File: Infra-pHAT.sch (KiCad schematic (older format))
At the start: 20 parts, among them Q1 BC817, U1 CAT24C32WI-GT3

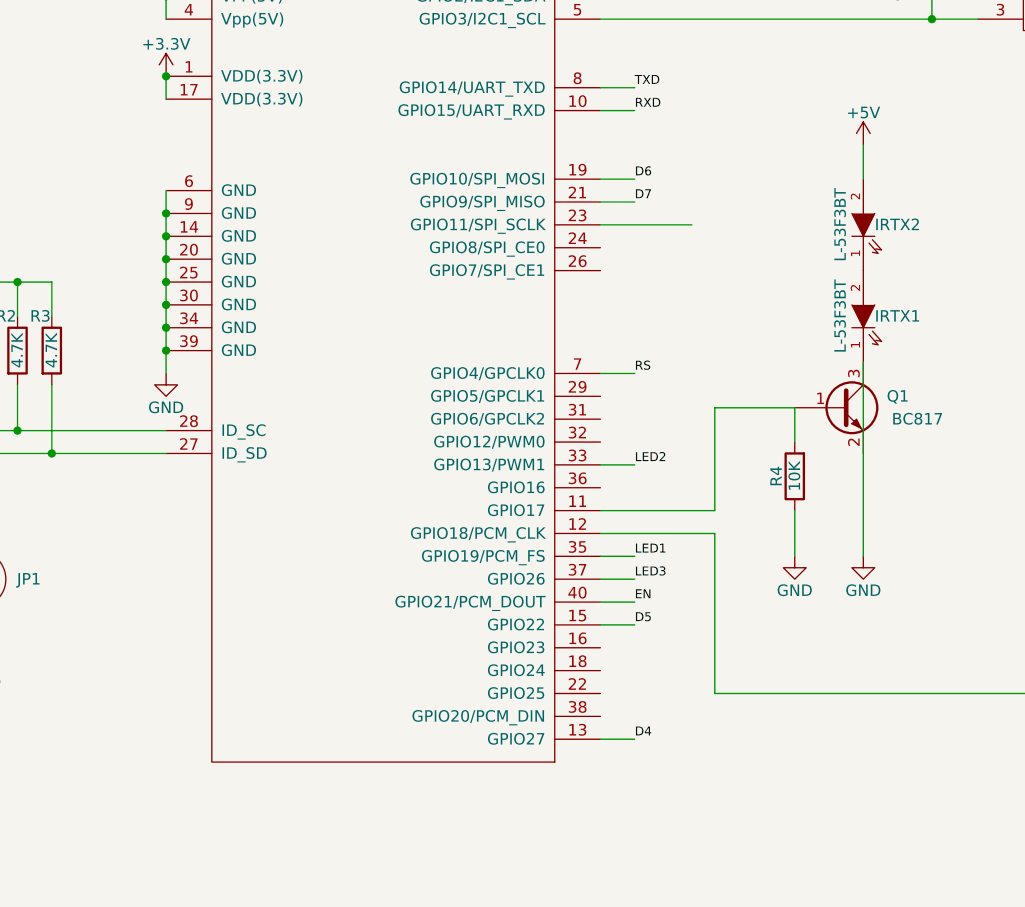
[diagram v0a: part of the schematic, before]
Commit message: Fix position of mounting holes and pin header
Fix wiring of transistor for IR leds

Signed-off-by: Rangel Ivanov <rangelivanov88@gmail.com>
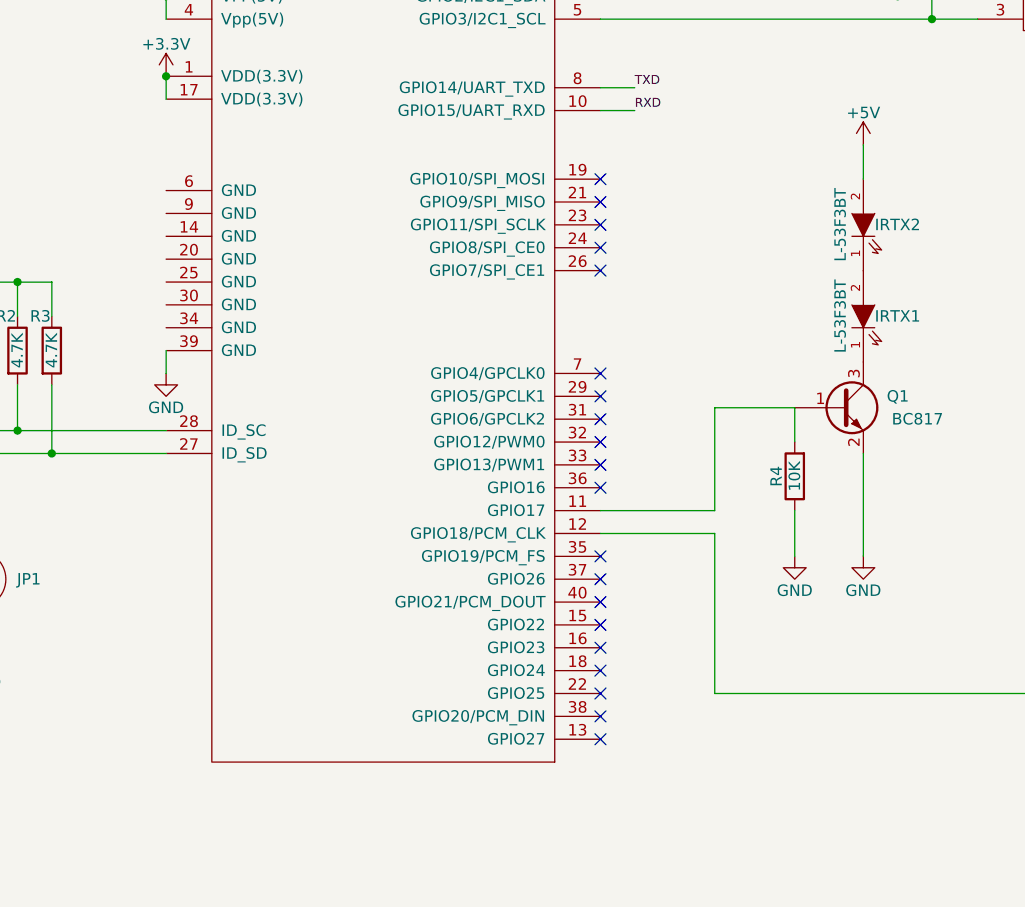
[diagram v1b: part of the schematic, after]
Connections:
- net GND: now also Q1.2 (E); no longer IRTX1.1 (K), Q1.3 (C), RASP_CONN1.14 (GND), RASP_CONN1.20 (GND), RASP_CONN1.25 (GND), RASP_CONN1.30 (GND), RASP_CONN1.34 (GND), RASP_CONN1.6 (GND), RASP_CONN1.9 (GND)
- net D4: no longer names the net of RASP_CONN1.13 (GPIO27)
- net D5: no longer names the net of RASP_CONN1.15 (GPIO22)
- net D6: no longer names the net of RASP_CONN1.19 (GPIO10/SPI_MOSI)
- net D7: no longer names the net of RASP_CONN1.21 (GPIO9/SPI_MISO)
- net EN: no longer names the net of RASP_CONN1.40 (GPIO21/PCM_DOUT)
- net LED1: no longer names the net of RASP_CONN1.35 (GPIO19/PCM_FS)
- net LED2: no longer names the net of RASP_CONN1.33 (GPIO13/PWM1)
- net LED3: no longer names the net of RASP_CONN1.37 (GPIO26)
- net RS: no longer names the net of RASP_CONN1.7 (GPIO4/GPCLK0)
- new net: IRTX1.1 (K), Q1.3 (C)
- no-connect marks 0 -> 20
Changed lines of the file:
@@
 EESchema Schematic File Version 2
-LIBS:power
-LIBS:device
-LIBS:transistors
-LIBS:conn
-LIBS:linear
-LIBS:regul
-LIBS:74xx
-LIBS:cmos4000
-LIBS:adc-dac
-LIBS:memory
-LIBS:xilinx
-LIBS:microcontrollers
-LIBS:dsp
-LIBS:microchip
-LIBS:analog_switches
-LIBS:motorola
-LIBS:texas
-LIBS:intel
-LIBS:audio
-LIBS:interface
-LIBS:digital-audio
-LIBS:philips
-LIBS:display
-LIBS:cypress
-LIBS:siliconi
-LIBS:opto
-LIBS:atmel
-LIBS:contrib
-LIBS:valves
 LIBS:mylibrary
 LIBS:Infra-pHAT-cache
@@
 $EndComp
 Wire Wire Line
-	3450 2650 3450 3450
-Connection ~ 3450 2750
-Connection ~ 3450 2850
-Connection ~ 3450 2950
-Connection ~ 3450 3050
-Connection ~ 3450 3150
-Connection ~ 3450 3250
-Connection ~ 3450 3350
-Wire Wire Line
 	3450 2150 3450 2250
 Connection ~ 3450 2150
@@
 	0    1    1    0
 $EndComp
-Wire Wire Line
-	6500 3400 6500 4250
 $Comp
 L R R4
@@
 	7850 5150 7900 5150
 Wire Wire Line
-	5350 4550 5500 4550
-Wire Wire Line
-	5350 3850 5500 3850
-Text Label 5500 4550 0    39   ~ 0
-D5
-Wire Wire Line
 	7550 5150 7500 5150
 Wire Wire Line
@@
 	7400 4850 7400 4750
 Wire Wire Line
-	5350 2800 5750 2800
-Wire Wire Line
-	5350 5050 5500 5050
-Text Label 5500 5050 0    39   ~ 0
-D4
-Wire Wire Line
-	5350 2600 5500 2600
-Text Label 5500 2600 0    39   ~ 0
-D6
-Wire Wire Line
-	5350 2700 5500 2700
-Text Label 5500 2700 0    39   ~ 0
-D7
-Wire Wire Line
 	6500 2450 6500 2600
-Wire Wire Line
-	5350 4250 5500 4250
-Text Label 5500 4250 0    39   ~ 0
-LED1
-Text Label 5500 3850 0    39   ~ 0
-LED2
-Wire Wire Line
-	5350 4350 5500 4350
-Text Label 5500 4350 0    39   ~ 0
-LED3
-Wire Wire Line
-	5350 4450 5500 4450
-Text Label 5500 4450 0    39   ~ 0
-EN
 $Comp
 L CONN_01X04 UART1
@@
 	5850 4050 5350 4050
 Wire Wire Line
-	5350 3450 5500 3450
-Text Label 5500 3450 0    39   ~ 0
-RS
-Wire Wire Line
 	6800 900  6800 1900
 Wire Wire Line
@@
 Wire Wire Line
 	6200 4050 6200 4250
+Wire Wire Line
+	6500 3800 6500 4250
+NoConn ~ 5350 5050
+NoConn ~ 5350 4950
+NoConn ~ 5350 4850
+NoConn ~ 5350 4750
+NoConn ~ 5350 4650
+NoConn ~ 5350 4550
+NoConn ~ 5350 4450
+NoConn ~ 5350 4350
+NoConn ~ 5350 4250
+NoConn ~ 5350 3550
+NoConn ~ 5350 3650
+NoConn ~ 5350 3750
+NoConn ~ 5350 3850
+NoConn ~ 5350 3950
+NoConn ~ 5350 3450
+NoConn ~ 5350 2900
+NoConn ~ 5350 3000
+NoConn ~ 5350 2800
+NoConn ~ 5350 2600
+NoConn ~ 5350 2700
+Wire Wire Line
+	3450 3350 3450 3450
 $EndSCHEMATC

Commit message: Add filled zone for front layer (GND net)
Route RX/TX for UART connector

Signed-off-by: Rangel Ivanov <rangelivanov88@gmail.com>
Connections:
- net GND: now also RASP_CONN1.14 (GND), RASP_CONN1.20 (GND), RASP_CONN1.25 (GND), RASP_CONN1.30 (GND), RASP_CONN1.34 (GND), RASP_CONN1.6 (GND), RASP_CONN1.9 (GND)
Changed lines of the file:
@@
 	1    0    0    -1
 $EndComp
-Wire Wire Line
-	950  3500 800  3500
-Wire Wire Line
-	800  3500 800  3950
-Wire Wire Line
-	950  3600 800  3600
-Connection ~ 800  3600
-Wire Wire Line
-	950  3700 800  3700
-Connection ~ 800  3700
-Wire Wire Line
-	950  3800 800  3800
-Connection ~ 800  3800
 $Comp
 L GND #PWR02
@@
 	0    1    1    0
 $EndComp
-Wire Wire Line
-	2200 3500 2050 3500
 $Comp
 L +3.3V #PWR03
@@
 	1    0    0    -1
 $EndComp
-Connection ~ 2200 3050
-Wire Wire Line
-	2950 3050 2950 3200
-Wire Wire Line
-	2800 3050 2800 3200
-Connection ~ 2800 3050
-Wire Wire Line
-	2650 3200 2650 3050
-Connection ~ 2650 3050
-Wire Wire Line
-	2200 3050 2950 3050
-Wire Wire Line
-	2050 3600 2650 3600
-Wire Wire Line
-	2650 3500 2650 4050
-Wire Wire Line
-	2800 3700 2800 3500
-Wire Wire Line
-	2950 3800 2950 3500
 $Comp
 L GND #PWR04
@@
 	1    0    0    -1
 $EndComp
-Connection ~ 2950 3800
-Connection ~ 2800 3700
 $Comp
 L Raspberry_PI RASP_CONN1
@@
 	1    0    0    -1
 $EndComp
-Wire Wire Line
-	2200 2700 2200 3500
-Connection ~ 2650 3600
 $Comp
 L LED IRTX1
@@
 	0    1    1    0
 $EndComp
-Wire Wire Line
-	7500 4750 7500 5300
 $Comp
 L CP C2
@@
 	1    0    0    -1
 $EndComp
-Connection ~ 7500 5150
 $Comp
 L +3.3V #PWR08
@@
 	1    0    0    -1
 $EndComp
-Wire Wire Line
-	3450 2150 3450 2250
-Connection ~ 3450 2150
 $Comp
 L +3.3V #PWR010
@@
 	1    0    0    -1
 $EndComp
-Connection ~ 3450 1800
 $Comp
 L +5V #PWR011
@@
 	1    0    0    -1
 $EndComp
-Wire Wire Line
-	3450 1800 3450 1900
 $Comp
 L I2C_SENS_1 SENS1
@@
 	1    0    0    -1
 $EndComp
-Wire Wire Line
-	5350 1800 7000 1800
-Wire Wire Line
-	5350 1900 7000 1900
-Connection ~ 6650 1800
-Connection ~ 6800 1900
 $Comp
 L GND #PWR012
@@
 	1    0    0    -1
 $EndComp
-Wire Wire Line
-	8050 900  8050 2100
-Wire Wire Line
-	8050 1900 7900 1900
 $Comp
 L +3.3V #PWR013
@@
 	1    0    0    -1
 $EndComp
-Connection ~ 7900 1800
 $Comp
 L Q_NPN_BEC Q1
@@
 	-1   0    0    1
 $EndComp
-Wire Wire Line
-	2050 3700 3450 3700
-Wire Wire Line
-	2050 3800 3450 3800
-Wire Wire Line
-	7850 5150 7900 5150
-Wire Wire Line
-	7550 5150 7500 5150
-Wire Wire Line
-	5350 4150 5850 4150
-Wire Wire Line
-	5850 4150 5850 4850
-Wire Wire Line
-	5850 4850 7400 4850
-Wire Wire Line
-	7400 4850 7400 4750
-Wire Wire Line
-	6500 2450 6500 2600
 $Comp
 L CONN_01X04 UART1
@@
 	1    0    0    -1
 $EndComp
-Wire Wire Line
-	8800 2400 8550 2400
 $Comp
 L GND #PWR015
@@
 	1    0    0    -1
 $EndComp
-Wire Wire Line
-	8550 2100 8800 2100
-Wire Wire Line
-	5350 2200 5500 2200
 Text Label 5500 2200 0    39   ~ 0
 TXD
-Wire Wire Line
-	5350 2300 5500 2300
 Text Label 5500 2300 0    39   ~ 0
 RXD
-Wire Wire Line
-	8800 2200 8550 2200
 Text Label 8550 2200 0    39   ~ 0
 TXD
-Wire Wire Line
-	8800 2300 8550 2300
 Text Label 8550 2300 0    39   ~ 0
 RXD
@@
 	1    0    0    -1
 $EndComp
-Connection ~ 7900 1200
-Connection ~ 7900 800
-Wire Wire Line
-	7900 900  8050 900
-Wire Wire Line
-	8050 1300 7900 1300
-Connection ~ 8050 1900
-Connection ~ 8050 1300
-Wire Wire Line
-	7000 800  6650 800
-Wire Wire Line
-	6200 1200 7000 1200
-Connection ~ 6650 1200
-Wire Wire Line
-	7000 900  6800 900
-Wire Wire Line
-	6350 1300 7000 1300
-Connection ~ 6800 1300
-Wire Wire Line
-	6350 1050 6350 1300
-Wire Wire Line
-	6200 1050 6200 1200
-Wire Wire Line
-	6050 750  6350 750
-Connection ~ 6200 750
 $Comp
 L +3.3V #PWR017
@@
 	0    -1   -1   0
 $EndComp
-Wire Wire Line
-	5850 4050 5350 4050
-Wire Wire Line
-	6800 900  6800 1900
-Wire Wire Line
-	6650 800  6650 1800
-Wire Wire Line
-	7900 700  7900 1800
 $Comp
 L LED IRTX2
@@
 	0    -1   -1   0
 $EndComp
-Wire Wire Line
-	5850 4050 5850 3600
-Wire Wire Line
-	5850 3600 6200 3600
-Wire Wire Line
-	6200 3600 6200 3750
 $Comp
 L GND #PWR018
@@
 	1    0    0    -1
 $EndComp
-Wire Wire Line
-	6200 4050 6200 4250
-Wire Wire Line
-	6500 3800 6500 4250
 NoConn ~ 5350 5050
 NoConn ~ 5350 4950
@@
 NoConn ~ 5350 2700
 Wire Wire Line
-	3450 3350 3450 3450
+	950  3500 800  3500
+Wire Wire Line
+	800  3500 800  3950
+Wire Wire Line
+	950  3600 800  3600
+Connection ~ 800  3600
+Wire Wire Line
+	950  3700 800  3700
+Connection ~ 800  3700
+Wire Wire Line
+	950  3800 800  3800
+Connection ~ 800  3800
+Wire Wire Line
+	2200 3500 2050 3500
+Connection ~ 2200 3050
+Wire Wire Line
+	2950 3050 2950 3200
+Wire Wire Line
+	2800 3050 2800 3200
+Connection ~ 2800 3050
+Wire Wire Line
+	2650 3200 2650 3050
+Connection ~ 2650 3050
+Wire Wire Line
+	2200 3050 2950 3050
+Wire Wire Line
+	2050 3600 2650 3600
+Wire Wire Line
+	2650 3500 2650 4050
+Wire Wire Line
+	2800 3700 2800 3500
+Wire Wire Line
+	2950 3800 2950 3500
+Connection ~ 2950 3800
+Connection ~ 2800 3700
+Wire Wire Line
+	2200 2700 2200 3500
+Connection ~ 2650 3600
+Wire Wire Line
+	7500 4750 7500 5300
+Connection ~ 7500 5150
+Wire Wire Line
+	3450 2150 3450 2250
+Connection ~ 3450 2150
+Connection ~ 3450 1800
+Wire Wire Line
+	3450 1800 3450 1900
+Wire Wire Line
+	5350 1800 7000 1800
+Wire Wire Line
+	5350 1900 7000 1900
+Connection ~ 6650 1800
+Connection ~ 6800 1900
+Wire Wire Line
+	8050 900  8050 2100
+Wire Wire Line
+	8050 1900 7900 1900
+Connection ~ 7900 1800
+Wire Wire Line
+	2050 3700 3450 3700
+Wire Wire Line
+	2050 3800 3450 3800
+Wire Wire Line
+	7850 5150 7900 5150
+Wire Wire Line
+	7550 5150 7500 5150
+Wire Wire Line
+	5350 4150 5850 4150
+Wire Wire Line
+	5850 4150 5850 4850
+Wire Wire Line
+	5850 4850 7400 4850
+Wire Wire Line
+	7400 4850 7400 4750
+Wire Wire Line
+	6500 2450 6500 2600
+Wire Wire Line
+	8800 2400 8550 2400
+Wire Wire Line
+	8550 2100 8800 2100
+Wire Wire Line
+	5350 2200 5500 2200
+Wire Wire Line
+	5350 2300 5500 2300
+Wire Wire Line
+	8800 2200 8550 2200
+Wire Wire Line
+	8800 2300 8550 2300
+Connection ~ 7900 1200
+Connection ~ 7900 800
+Wire Wire Line
+	7900 900  8050 900
+Wire Wire Line
+	8050 1300 7900 1300
+Connection ~ 8050 1900
+Connection ~ 8050 1300
+Wire Wire Line
+	7000 800  6650 800
+Wire Wire Line
+	6200 1200 7000 1200
+Connection ~ 6650 1200
+Wire Wire Line
+	7000 900  6800 900
+Wire Wire Line
+	6350 1300 7000 1300
+Connection ~ 6800 1300
+Wire Wire Line
+	6350 1050 6350 1300
+Wire Wire Line
+	6200 1050 6200 1200
+Wire Wire Line
+	6050 750  6350 750
+Connection ~ 6200 750
+Wire Wire Line
+	5850 4050 5350 4050
+Wire Wire Line
+	6800 900  6800 1900
+Wire Wire Line
+	6650 800  6650 1800
+Wire Wire Line
+	7900 700  7900 1800
+Wire Wire Line
+	5850 4050 5850 3600
+Wire Wire Line
+	5850 3600 6200 3600
+Wire Wire Line
+	6200 3600 6200 3750
+Wire Wire Line
+	6200 4050 6200 4250
+Wire Wire Line
+	6500 3800 6500 4250
+Wire Wire Line
+	3450 2650 3450 3450
+Connection ~ 3450 2750
+Connection ~ 3450 2850
+Connection ~ 3450 2950
+Connection ~ 3450 3050
+Connection ~ 3450 3150
+Connection ~ 3450 3350
+Connection ~ 3450 3250
 $EndSCHEMATC

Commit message: Infra-pHAT.pro: remap symbols
Remap KiCad symbols.

Signed-off-by: Leon Anavi <leon@anavi.org>
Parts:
- C1: symbol C -> Infra-pHAT-rescue:C
- C2: symbol CP -> Infra-pHAT-rescue:CP
- IRRX1: symbol TSOP382 -> mylibrary:TSOP382
- IRTX1, IRTX2: symbol LED -> Infra-pHAT-rescue:LED
- JP1: symbol JUMPER -> Infra-pHAT-rescue:JUMPER
- Q1: symbol Q_NPN_BEC -> Infra-pHAT-rescue:Q_NPN_BEC
- R1, R2, R3, R4, R5, R6, R7: symbol R -> Infra-pHAT-rescue:R
- RASP_CONN1: symbol Raspberry_PI -> mylibrary:Raspberry_PI
- SENS1, SENS2, SENS3: symbol I2C_SENS_1 -> mylibrary:I2C_SENS_1
- U1: symbol CAT24C32WI-GT3 -> mylibrary:CAT24C32WI-GT3
- UART1: symbol CONN_01X04 -> Infra-pHAT-rescue:CONN_01X04
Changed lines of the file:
@@
-EESchema Schematic File Version 2
-LIBS:mylibrary
-LIBS:Infra-pHAT-cache
-EELAYER 25 0
+EESchema Schematic File Version 4
+EELAYER 30 0
 EELAYER END
 $Descr A4 11693 8268
@@
 $EndDescr
 $Comp
-L CAT24C32WI-GT3 U1
+L mylibrary:CAT24C32WI-GT3 U1
 U 1 1 56FB5761
 P 1500 3300
@@
 $EndComp
 $Comp
-L R R1
+L Infra-pHAT-rescue:R R1
 U 1 1 56FB57DD
 P 2650 3350
@@
 $EndComp
 $Comp
-L R R2
+L Infra-pHAT-rescue:R R2
 U 1 1 56FB589D
 P 2800 3350
@@
 $EndComp
 $Comp
-L R R3
+L Infra-pHAT-rescue:R R3
 U 1 1 56FB5912
 P 2950 3350
@@
 $EndComp
 $Comp
-L C C1
+L Infra-pHAT-rescue:C C1
 U 1 1 56FB5967
 P 2050 3050
@@
 $EndComp
 $Comp
-L GND #PWR01
+L power:GND #PWR01
 U 1 1 56FB5AA8
 P 800 3950
@@
 $EndComp
 $Comp
-L GND #PWR02
+L power:GND #PWR02
 U 1 1 56FB5B93
 P 1900 3050
@@
 $EndComp
 $Comp
-L +3.3V #PWR03
+L power:+3.3V #PWR03
 U 1 1 56FB5F37
 P 2200 2700
@@
 $EndComp
 $Comp
-L GND #PWR04
+L power:GND #PWR04
 U 1 1 56FB60BD
 P 2650 4650
@@
 $EndComp
 $Comp
-L Raspberry_PI RASP_CONN1
+L mylibrary:Raspberry_PI RASP_CONN1
 U 1 1 56FB7C7A
 P 4400 1700
@@
 $EndComp
 $Comp
-L LED IRTX1
+L Infra-pHAT-rescue:LED IRTX1
 U 1 1 56FCCD5F
 P 6500 3200
@@
 $EndComp
 $Comp
-L GND #PWR05
+L power:GND #PWR05
 U 1 1 56FCD5E9
 P 6500 4250
@@
 $EndComp
 $Comp
-L TSOP382 IRRX1
+L mylibrary:TSOP382 IRRX1
 U 1 1 56FCDD28
 P 7250 4550
@@
 $EndComp
 $Comp
-L GND #PWR06
+L power:GND #PWR06
 U 1 1 56FCDFD8
 P 7600 4750
@@
 $EndComp
 $Comp
-L R R5
+L Infra-pHAT-rescue:R R5
 U 1 1 56FCE3CD
 P 7700 5150
@@
 $EndComp
 $Comp
-L CP C2
+L Infra-pHAT-rescue:CP C2
 U 1 1 56FCE773
 P 7500 5450
@@
 $EndComp
 $Comp
-L GND #PWR07
+L power:GND #PWR07
 U 1 1 56FCE7D8
 P 7500 5600
@@
 $EndComp
 $Comp
-L +3.3V #PWR08
+L power:+3.3V #PWR08
 U 1 1 56FCEA80
 P 7900 5150
@@
 $EndComp
 $Comp
-L GND #PWR09
+L power:GND #PWR09
 U 1 1 56FD1B71
 P 3450 3450
@@
 $EndComp
 $Comp
-L +3.3V #PWR010
+L power:+3.3V #PWR010
 U 1 1 56FD2267
 P 3450 2150
@@
 $EndComp
 $Comp
-L +5V #PWR011
+L power:+5V #PWR011
 U 1 1 56FF1D94
 P 3450 1800
@@
 $EndComp
 $Comp
-L I2C_SENS_1 SENS1
+L mylibrary:I2C_SENS_1 SENS1
 U 1 1 5704A9C3
 P 7200 1700
@@
 $EndComp
 $Comp
-L GND #PWR012
+L power:GND #PWR012
 U 1 1 5704B80C
 P 8050 2100
@@
 $EndComp
 $Comp
-L +3.3V #PWR013
+L power:+3.3V #PWR013
 U 1 1 5704BA43
 P 7900 700
@@
 $EndComp
 $Comp
-L Q_NPN_BEC Q1
+L Infra-pHAT-rescue:Q_NPN_BEC Q1
 U 1 1 570BF19F
 P 6400 3600
@@
 $EndComp
 $Comp
-L +5V #PWR014
+L power:+5V #PWR014
 U 1 1 570BFB30
 P 6500 2450
@@
 $EndComp
 $Comp
-L R R6
+L Infra-pHAT-rescue:R R6
 U 1 1 570C0762
 P 6200 900
@@
 $EndComp
 $Comp
-L R R7
+L Infra-pHAT-rescue:R R7
 U 1 1 570C0BD5
 P 6350 900
@@
 $EndComp
 $Comp
-L JUMPER JP1
+L Infra-pHAT-rescue:JUMPER JP1
 U 1 1 570C5478
 P 2650 4350
@@
 $EndComp
 $Comp
-L R R4
+L Infra-pHAT-rescue:R R4
 U 1 1 570BEF32
 P 6200 3900
@@
 $EndComp
 $Comp
-L CONN_01X04 UART1
+L Infra-pHAT-rescue:CONN_01X04 UART1
 U 1 1 574EB04E
 P 9000 2250
@@
 $EndComp
 $Comp
-L GND #PWR015
+L power:GND #PWR015
 U 1 1 574EBFC1
 P 8550 2400
@@
 $EndComp
 $Comp
-L +3.3V #PWR016
+L power:+3.3V #PWR016
 U 1 1 574EC177
 P 8550 2100
@@
 RXD
 $Comp
-L I2C_SENS_1 SENS2
+L mylibrary:I2C_SENS_1 SENS2
 U 1 1 5752A123
 P 7200 1100
@@
 $EndComp
 $Comp
-L I2C_SENS_1 SENS3
+L mylibrary:I2C_SENS_1 SENS3
 U 1 1 5752A2F7
 P 7200 700
@@
 $EndComp
 $Comp
-L +3.3V #PWR017
+L power:+3.3V #PWR017
 U 1 1 5752AF07
 P 6050 750
@@
 $EndComp
 $Comp
-L LED IRTX2
+L Infra-pHAT-rescue:LED IRTX2
 U 1 1 5882BE41
 P 6500 2800
@@
 $EndComp
 $Comp
-L GND #PWR018
+L power:GND #PWR018
 U 1 1 5882D374
 P 6200 4250
@@
 	950  3500 800  3500
 Wire Wire Line
-	800  3500 800  3950
+	800  3500 800  3600
 Wire Wire Line
 	950  3600 800  3600
@@
 Connection ~ 2650 3050
 Wire Wire Line
-	2200 3050 2950 3050
+	2200 3050 2650 3050
 Wire Wire Line
 	2050 3600 2650 3600
 Wire Wire Line
-	2650 3500 2650 4050
+	2650 3500 2650 3600
 Wire Wire Line
 	2800 3700 2800 3500
@@
 Connection ~ 2800 3700
 Wire Wire Line
-	2200 2700 2200 3500
+	2200 2700 2200 3050
 Connection ~ 2650 3600
 Wire Wire Line
-	7500 4750 7500 5300
+	7500 4750 7500 5150
 Connection ~ 7500 5150
 Wire Wire Line
@@
 	3450 1800 3450 1900
 Wire Wire Line
-	5350 1800 7000 1800
-Wire Wire Line
-	5350 1900 7000 1900
+	5350 1800 6650 1800
+Wire Wire Line
+	5350 1900 6800 1900
 Connection ~ 6650 1800
 Connection ~ 6800 1900
 Wire Wire Line
-	8050 900  8050 2100
+	8050 900  8050 1300
 Wire Wire Line
 	8050 1900 7900 1900
-Connection ~ 7900 1800
-Wire Wire Line
-	2050 3700 3450 3700
-Wire Wire Line
-	2050 3800 3450 3800
+Wire Wire Line
+	2050 3700 2800 3700
+Wire Wire Line
+	2050 3800 2950 3800
 Wire Wire Line
 	7850 5150 7900 5150
@@
 	7000 800  6650 800
 Wire Wire Line
-	6200 1200 7000 1200
+	6200 1200 6650 1200
 Connection ~ 6650 1200
 Wire Wire Line
 	7000 900  6800 900
 Wire Wire Line
-	6350 1300 7000 1300
+	6350 1300 6800 1300
 Connection ~ 6800 1300
 Wire Wire Line
@@
 	6200 1050 6200 1200
 Wire Wire Line
-	6050 750  6350 750
+	6050 750  6200 750
 Connection ~ 6200 750
 Wire Wire Line
 	5850 4050 5350 4050
 Wire Wire Line
-	6800 900  6800 1900
-Wire Wire Line
-	6650 800  6650 1800
-Wire Wire Line
-	7900 700  7900 1800
+	6800 900  6800 1300
+Wire Wire Line
+	6650 800  6650 1200
+Wire Wire Line
+	7900 700  7900 800
 Wire Wire Line
 	5850 4050 5850 3600
@@
 	6500 3800 6500 4250
 Wire Wire Line
-	3450 2650 3450 3450
+	3450 2650 3450 2750
 Connection ~ 3450 2750
 Connection ~ 3450 2850
@@
 Connection ~ 3450 3350
 Connection ~ 3450 3250
+Wire Wire Line
+	800  3600 800  3700
+Wire Wire Line
+	800  3700 800  3800
+Wire Wire Line
+	800  3800 800  3950
+Wire Wire Line
+	2200 3050 2200 3500
+Wire Wire Line
+	2800 3050 2950 3050
+Wire Wire Line
+	2650 3050 2800 3050
+Wire Wire Line
+	2950 3800 3450 3800
+Wire Wire Line
+	2800 3700 3450 3700
+Wire Wire Line
+	2650 3600 2650 4050
+Wire Wire Line
+	7500 5150 7500 5300
+Wire Wire Line
+	6650 1800 7000 1800
+Wire Wire Line
+	6800 1900 7000 1900
+Wire Wire Line
+	7900 1200 7900 1800
+Wire Wire Line
+	7900 800  7900 1200
+Wire Wire Line
+	8050 1900 8050 2100
+Wire Wire Line
+	8050 1300 8050 1900
+Wire Wire Line
+	6650 1200 7000 1200
+Wire Wire Line
+	6650 1200 6650 1800
+Wire Wire Line
+	6800 1300 7000 1300
+Wire Wire Line
+	6800 1300 6800 1900
+Wire Wire Line
+	6200 750  6350 750
+Wire Wire Line
+	3450 2750 3450 2850
+Wire Wire Line
+	3450 2850 3450 2950
+Wire Wire Line
+	3450 2950 3450 3050
+Wire Wire Line
+	3450 3050 3450 3150
+Wire Wire Line
+	3450 3150 3450 3250
+Wire Wire Line
+	3450 3350 3450 3450
+Wire Wire Line
+	3450 3250 3450 3350
 $EndSCHEMATC

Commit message: Infra-pHAT.*: Add a current limiting resistor
Add a current limiting resistor for the IR LEDs.

Suggested-by: Norman Rasmussen <norman@rasmussen.co.za>
Signed-off-by: Leon Anavi <leon@anavi.org>
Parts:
- added R8: 36R, Resistors_SMD:R_0603_HandSoldering, symbol Device:R
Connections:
- net +5V: now also R8.1; no longer IRTX2.2 (A)
- new net: IRTX2.2 (A), R8.2
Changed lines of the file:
@@
 L power:+5V #PWR014
 U 1 1 570BFB30
-P 6500 2450
-F 0 "#PWR014" H 6500 2300 50  0001 C CNN
-F 1 "+5V" H 6500 2590 50  0000 C CNN
-F 2 "" H 6500 2450 50  0000 C CNN
-F 3 "" H 6500 2450 50  0000 C CNN
-	1    6500 2450
+P 6500 2150
+F 0 "#PWR014" H 6500 2000 50  0001 C CNN
+F 1 "+5V" H 6500 2290 50  0000 C CNN
+F 2 "" H 6500 2150 50  0000 C CNN
+F 3 "" H 6500 2150 50  0000 C CNN
+	1    6500 2150
 	1    0    0    -1
 $EndComp
@@
 Wire Wire Line
 	3450 3250 3450 3350
+$Comp
+L Device:R R8
+U 1 1 6260EFB5
+P 6500 2300
+F 0 "R8" H 6570 2346 50  0000 L CNN
+F 1 "36R" H 6570 2255 50  0000 L CNN
+F 2 "Resistors_SMD:R_0603_HandSoldering" V 6430 2300 50  0001 C CNN
+F 3 "~" H 6500 2300 50  0001 C CNN
+	1    6500 2300
+	1    0    0    -1
+$EndComp
 $EndSCHEMATC
